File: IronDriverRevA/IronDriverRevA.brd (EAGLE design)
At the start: 100 x 100 mm, 33 parts, among them IC1 PIC18F2550, IC2 TL074P, IC3 7805TV, IC4 TL072P, Q1 BC557C

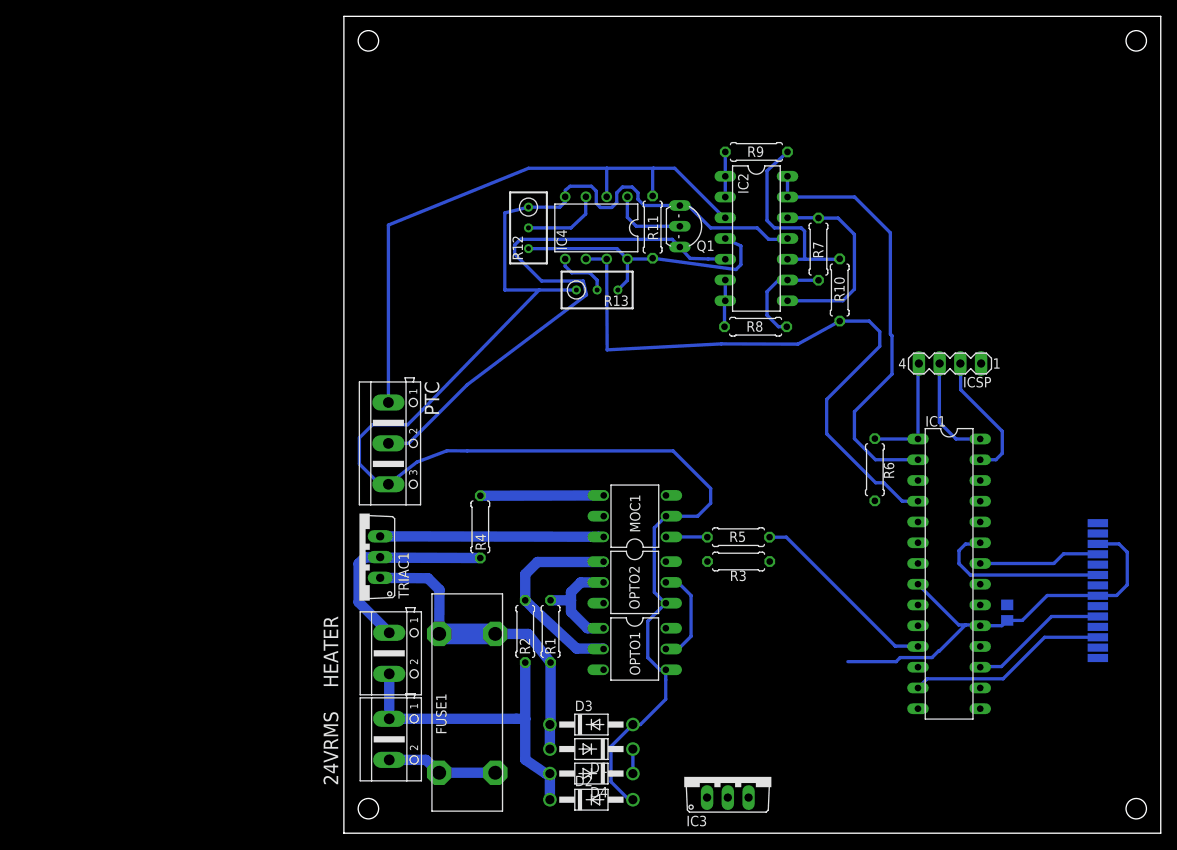
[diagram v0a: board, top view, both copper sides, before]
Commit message: Routing
DCDC added
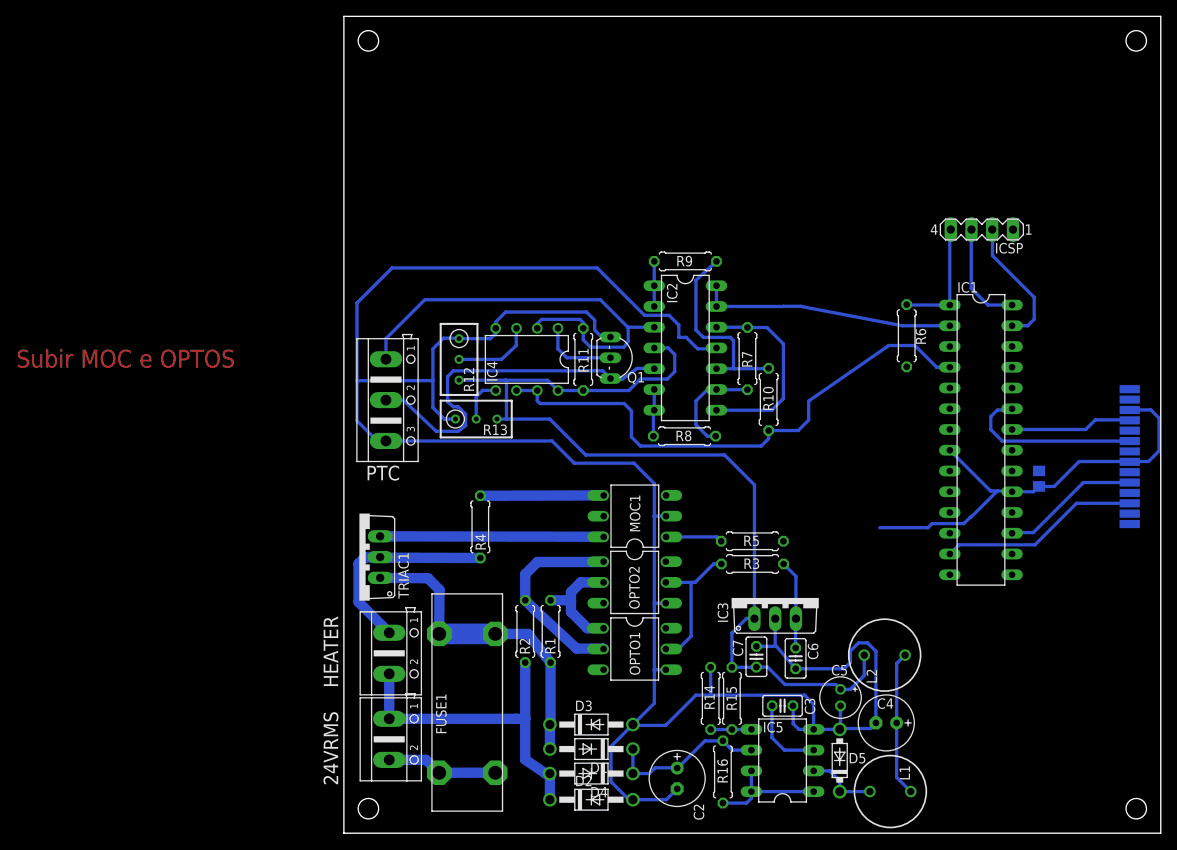
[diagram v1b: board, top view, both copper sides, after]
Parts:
- added C2: 100uF @ 35V, rcl:E2,5-7
- added C3: 200pF, rcl:C025-025X050
- added C4: 25uF, rcl:E2,5-7
- added C5: 100uF, rcl:E2-5
- added C6: .1uF @ 5V, rcl:C025-025X050
- added C7: .33uF @ 8V, rcl:C025-025X050
- added D5: 1N5819-T, diode:DO41-7.6
- added IC5: MC34063AP, mc34063:DIL08
- added L1: 210uH, rcl:6000-XXXX-RC
- added L2: 1uH, rcl:6000-XXXX-RC
- added R14: 2.4k, rcl:0207/7
- added R15: 13k, rcl:0207/7
- added R16: 1.5R, rcl:0207/7
- moved IC3 22.7 mm to (52.8, 28.8)
- moved R13 21.6 mm to (16.2, 50.7)
- moved R11 18.3 mm to (29.3, 58.0)
- moved IC4 18.2 mm to (22.4, 58.0)
- moved Q1 18.2 mm to (33.9, 58.2)
- moved R12 18.2 mm to (14.1, 58.0)
- moved ICSP 16.9 mm to (78.1, 73.9)
- moved J1 16.9 mm to (96.2, 46.1)
- moved R6 16.9 mm to (68.9, 60.9)
- moved C1 16.9 mm to (85.1, 43.4)
- moved IC1 16.9 mm to (78.0, 48.1)
- moved R9 16.0 mm to (41.8, 70.0)
- moved IC2 16.0 mm to (41.8, 59.4)
- moved R10 16.0 mm to (52.0, 53.1)
- moved R7 16.0 mm to (49.4, 58.1)
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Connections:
- removed net VCC: C1.1, IC1.20, J1.P$5, R3.2, R6.2
- new net +5V: C1.1, C6.1, IC1.20, IC3.3, J1.P$5, R3.2, R6.2
- new net N$13: D5.C, IC5.2, L1.1
- new net N$14: IC5.5, R14.2, R15.2
- new net N$15: IC5.1, IC5.7, IC5.8, R16.2
- new net N$18: C3.1, IC5.3
- new net N$20: C2.+, D1.C, D4.C, IC5.6, R16.1
- net +8V: now also C5.+, C7.1, IC3.1, L2.2, R15.1
- net GND: now also C2.-, C3.2, C4.-, C5.-, C6.2, C7.2, D5.A, IC3.2, IC5.4, R14.1
- net N$16: now also C4.+, L1.2, L2.1; no longer D1.C, D4.C
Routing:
- net GND: track 246.6 -> 336.0 mm
- net +8V: track 36.2 -> 117.1 mm
- net -PTC: track 70.6 -> 45.2 mm
- net HEATER: track 23.7 -> 0.00 mm
- net ADC_IN: track 53.0 -> 31.3 mm
- net N$20: track 0.00 -> 19.7 mm
- net +PTC: track 73.8 -> 55.4 mm
- net N$16: track 3.00 -> 17.8 mm
- net N$15: track 0.00 -> 14.7 mm
- net VGND: track 78.1 -> 65.9 mm
- net +5V: track 0.00 -> 10.9 mm
- net N$18: track 0.00 -> 9.66 mm
- net N$13: track 0.00 -> 8.71 mm
- net ZEROCROSSING: track 12.6 -> 18.1 mm
- net N$14: track 0.00 -> 5.00 mm
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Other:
- board text added: "Subir MOC e OPTOS"
